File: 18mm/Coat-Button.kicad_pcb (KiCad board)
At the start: 2 copper layers, 18 x 18 mm, 44 parts, among them IC1 MADW__ATTINY13-MM, P1 CONN_1, P2 CONN_1, P3 CONN_1, P4 CONN_1, Q1 DMG1012T, Q2 DMG1012T

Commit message: Modified SOT523 footprints to allow easier solder bridges.
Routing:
- net Net-<Q1-Pad3>: track 46.9 -> 48.1 mm
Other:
- board text added: "0.22.c"
- board text removed: "0.22.b"

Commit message: Tweaked changes in previous commit.
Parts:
- added JP2: JUMPER, MADW__R0402, F.Cu at (70.6, 62.8)
- added JP3: JUMPER, MADW__R0402, B.Cu at (70.2, 62.0)
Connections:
- net Net-<LED1-Pad2> renamed Net_LED1-Pad2_
- net Net-<LED1-Pad3> renamed Net_LED1-Pad3_
- net Net-<LED2-Pad2> renamed Net_LED2-Pad2_
- net Net-<LED2-Pad3> renamed Net_LED2-Pad3_
- net Net-<LED3-Pad2> renamed Net_LED3-Pad2_
- net Net-<LED3-Pad3> renamed Net_LED3-Pad3_
- net Net-<LED4-Pad2> renamed Net_LED4-Pad2_
- net Net-<LED4-Pad3> renamed Net_LED4-Pad3_
- net Net-<LED5-Pad2> renamed Net_LED5-Pad2_
- net Net-<LED5-Pad3> renamed Net_LED5-Pad3_
- net Net-<LED6-Pad2> renamed Net_LED6-Pad2_
- net Net-<LED6-Pad3> renamed Net_LED6-Pad3_
- net Net-<LED7-Pad2> renamed Net_LED7-Pad2_
- net Net-<LED7-Pad3> renamed Net_LED7-Pad3_
- net Net-<LED8-Pad2> renamed Net_LED8-Pad2_
- net Net-<LED8-Pad3> renamed Net_LED8-Pad3_
- Q1 pad 3: Net-<Q1-Pad3> -> /gate_a
- Q2 pad 3: Net-<Q2-Pad3> -> /gate_b
- R1 pad 1: Net-<Q2-Pad3> -> /gate_b
- R1.1 pad 1: Net-<Q1-Pad3> -> /gate_a
- R1.2 pad 2: Net-<Q1-Pad3> -> /gate_a
- R2 pad 1: Net-<Q2-Pad3> -> /gate_b
- R2.1 pad 1: Net-<Q1-Pad3> -> /gate_a
- R2.2 pad 2: Net-<Q1-Pad3> -> /gate_a
- R3 pad 1: Net-<Q2-Pad3> -> /gate_b
- R3.1 pad 1: Net-<Q1-Pad3> -> /gate_a
- R3.2 pad 2: Net-<Q1-Pad3> -> /gate_a
- R4 pad 1: Net-<Q2-Pad3> -> /gate_b
- R4.1 pad 1: Net-<Q1-Pad3> -> /gate_a
- R4.2 pad 2: Net-<Q1-Pad3> -> /gate_a
- R5 pad 1: Net-<Q2-Pad3> -> /gate_b
- R5.1 pad 1: Net-<Q1-Pad3> -> /gate_a
- R5.2 pad 2: Net-<Q1-Pad3> -> /gate_a
- R6 pad 1: Net-<Q2-Pad3> -> /gate_b
- R6.1 pad 1: Net-<Q1-Pad3> -> /gate_a
- R6.2 pad 2: Net-<Q1-Pad3> -> /gate_a
- R7 pad 1: Net-<Q2-Pad3> -> /gate_b
- R7.1 pad 1: Net-<Q1-Pad3> -> /gate_a
- R7.2 pad 2: Net-<Q1-Pad3> -> /gate_a
- R8 pad 1: Net-<Q2-Pad3> -> /gate_b
- R8.1 pad 1: Net-<Q1-Pad3> -> /gate_a
- R8.2 pad 2: Net-<Q1-Pad3> -> /gate_a
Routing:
- net /gate_a: track 1.42 -> 51.6 mm, vias 0 -> 8
- net Net-<Q1-Pad3>: track 48.1 -> 0.00 mm, vias 8 -> 0
- net /gate_b: track 3.32 -> 41.7 mm
- net Net-<Q2-Pad3>: track 37.4 -> 0.00 mm
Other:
- board text added: "0.23.a"
- board text removed: "0.22.c"

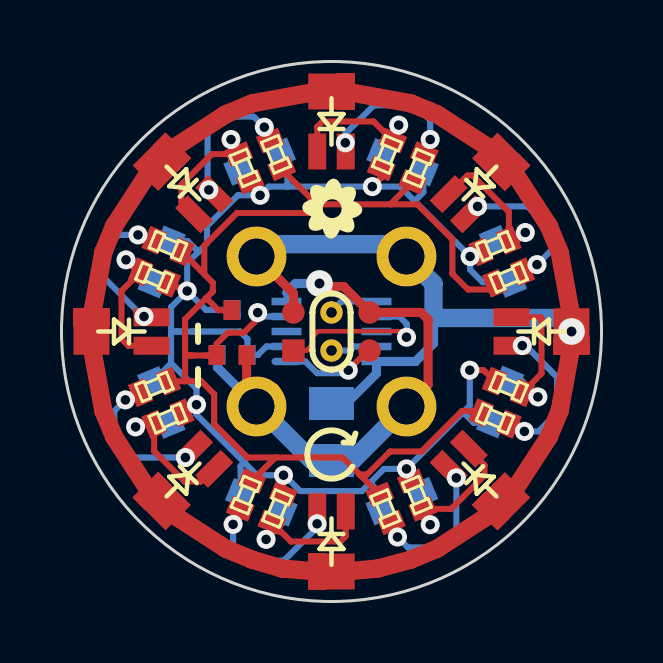
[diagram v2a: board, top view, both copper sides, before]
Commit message: Moved capacitor + tweaks.
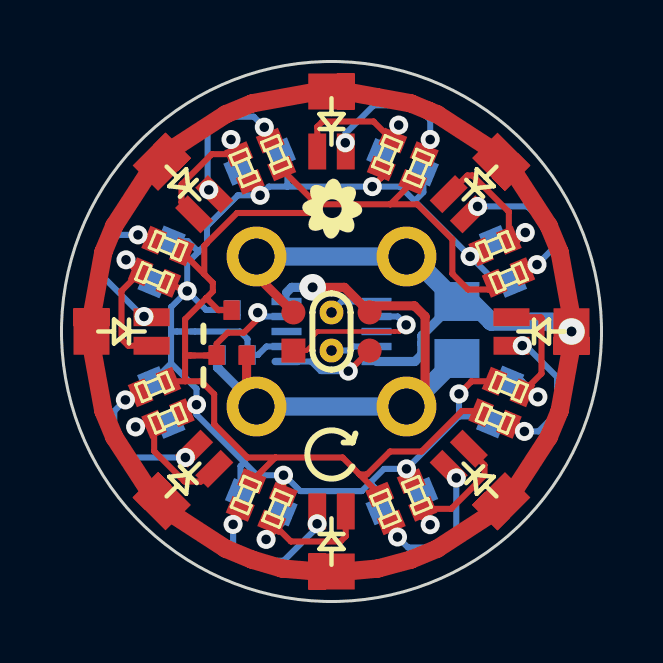
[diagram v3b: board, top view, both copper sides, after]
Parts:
- C1: value 4.7µF -> 100nF
- moved C1 5.39 mm to (79.2, 62.0)
- moved G2 0.28 mm to (82.1, 62.1)
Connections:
- net Net_LED1-Pad2_ renamed Net-(LED1-Pad2)
- net Net_LED1-Pad3_ renamed Net-(LED1-Pad3)
- net Net_LED2-Pad2_ renamed Net-(LED2-Pad2)
- net Net_LED2-Pad3_ renamed Net-(LED2-Pad3)
- net Net_LED3-Pad2_ renamed Net-(LED3-Pad2)
- net Net_LED3-Pad3_ renamed Net-(LED3-Pad3)
- net Net_LED4-Pad2_ renamed Net-(LED4-Pad2)
- net Net_LED4-Pad3_ renamed Net-(LED4-Pad3)
- net Net_LED5-Pad2_ renamed Net-(LED5-Pad2)
- net Net_LED5-Pad3_ renamed Net-(LED5-Pad3)
- net Net_LED6-Pad2_ renamed Net-(LED6-Pad2)
- net Net_LED6-Pad3_ renamed Net-(LED6-Pad3)
- net Net_LED7-Pad2_ renamed Net-(LED7-Pad2)
- net Net_LED7-Pad3_ renamed Net-(LED7-Pad3)
- net Net_LED8-Pad2_ renamed Net-(LED8-Pad2)
- net Net_LED8-Pad3_ renamed Net-(LED8-Pad3)
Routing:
- net VCC: track 71.2 -> 68.3 mm
- net /gate_a: track 51.6 -> 50.9 mm
- net GND: track 19.4 -> 20.1 mm
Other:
- board text added: "0.23.b"
- board text removed: "0.23.a"
